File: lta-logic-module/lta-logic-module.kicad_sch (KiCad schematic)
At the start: 9 parts

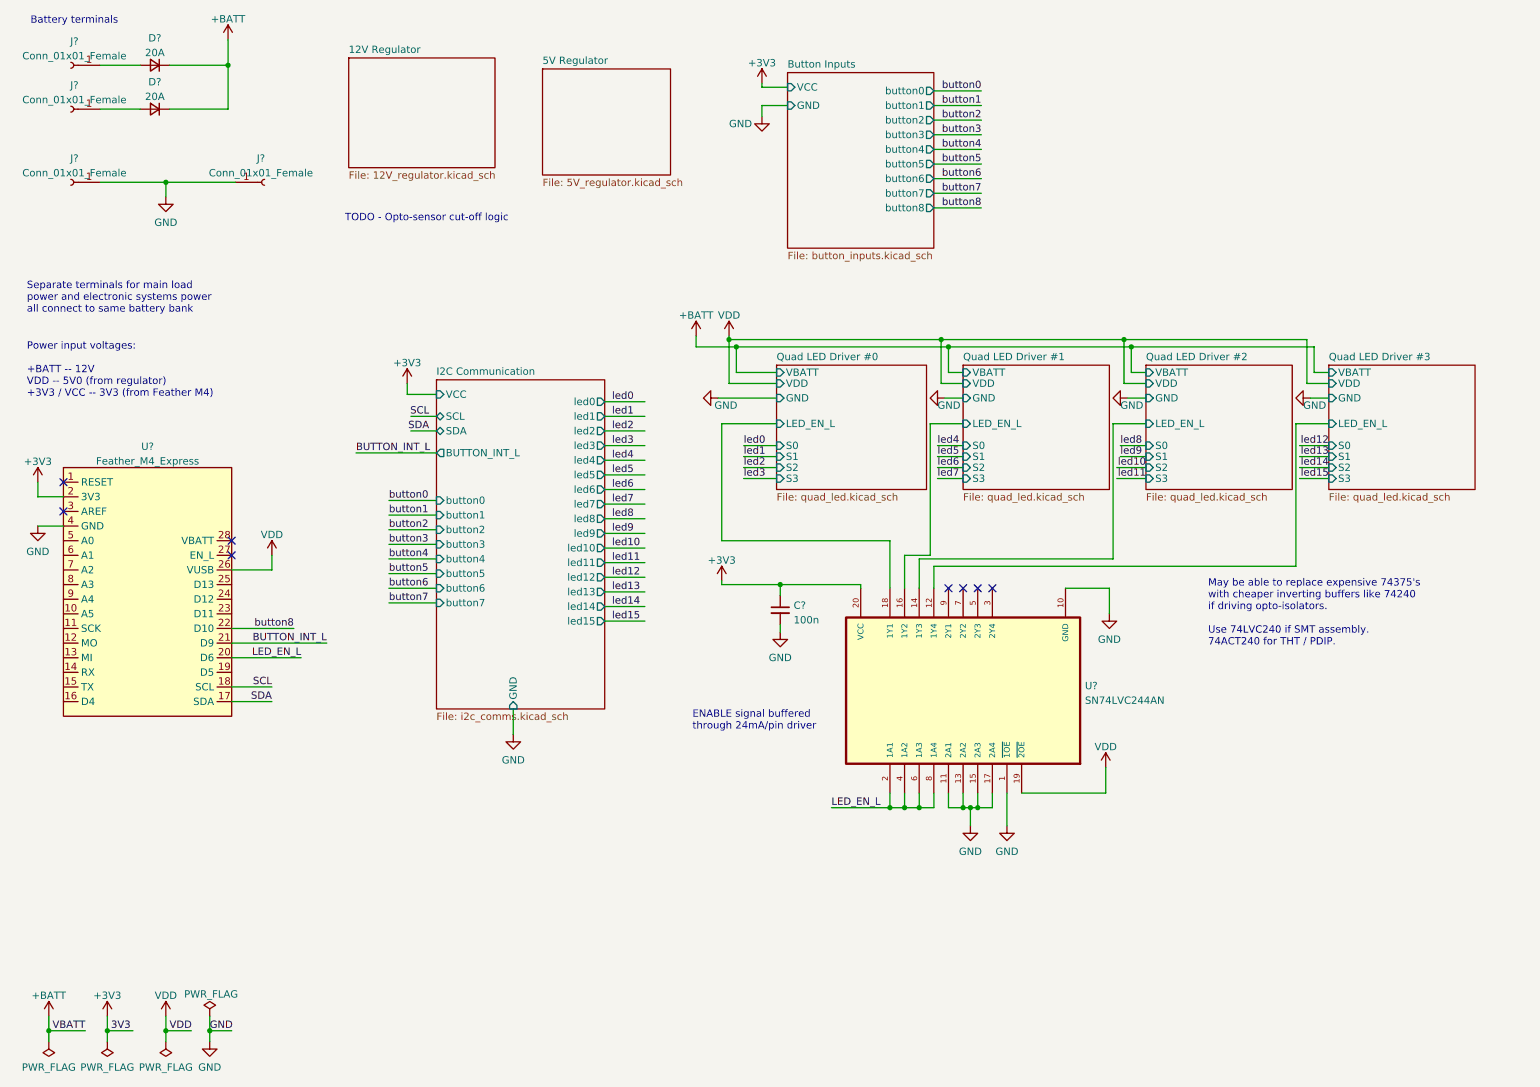
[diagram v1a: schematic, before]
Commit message: Full sketch of logic module schematic.
- Add button inputs
- Add LED signal driver / PWM combination
- Add 5V regulator based on LM2592
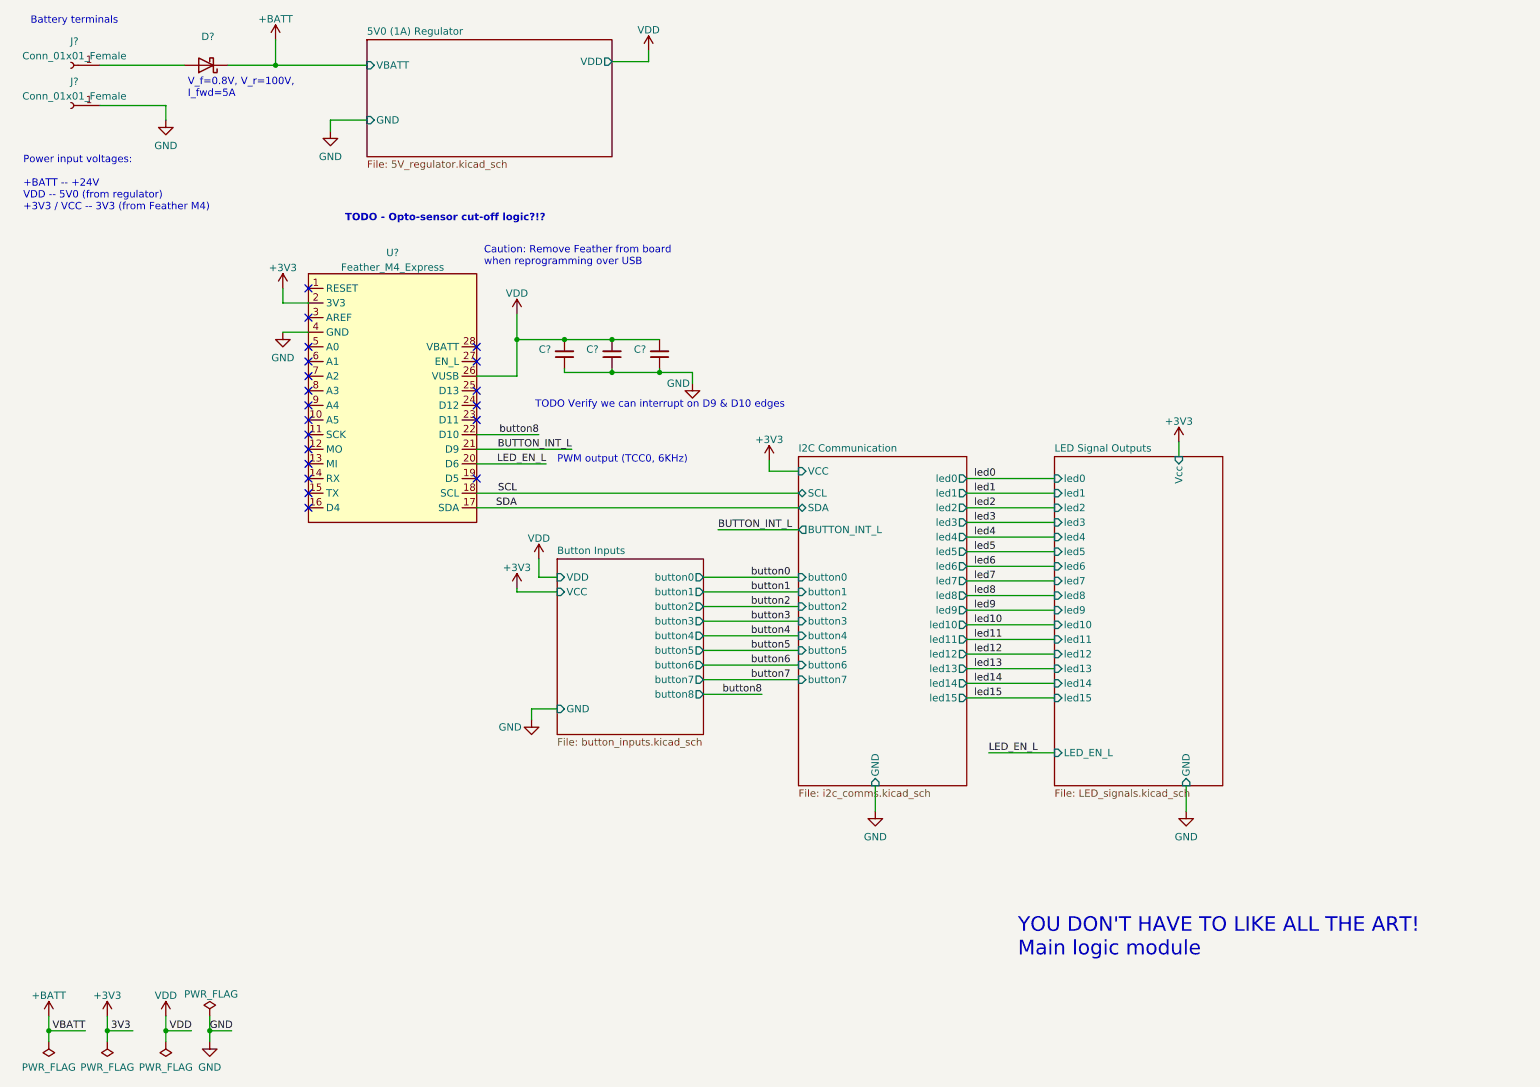
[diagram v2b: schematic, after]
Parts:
- removed C?: 100n, symbol Device:C_Small
- removed D? (x2): 20A, symbol Device:D_Small
- removed J? (x2): Conn_01x01_Female, symbol Connector:Conn_01x01_Female
- removed U?: SN74LVC244AN, Aaron_TI_Parts:TI_N_R-PDIP-T20, symbol Aaron-TI-Buffers:SN74LVC244AN
- added C? (x3): (no value), symbol Device:C_Small
- added D?: (no value), symbol Device:D_Schottky
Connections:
- net +BATT: now also D?.1 (K)
- net GND: now also C?.1, C?.1, C?.1
- net VDD: now also C?.2, C?.2, C?.2
- net at J?.1 (Pin_1): now also D?.2 (A)
- no-connect marks 8 -> 20
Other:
- sheet 5V Regulator renamed 5V0 (1A) Regulator
- removed sheet 12V Regulator
- removed sheet Quad LED Driver #0
- removed sheet Quad LED Driver #1
- removed sheet Quad LED Driver #2
- removed sheet Quad LED Driver #3
- added sheet LED Signal Outputs (LED_signals.kicad_sch)
- sheet 5V0 (1A) Regulator ports: added GND, VBATT, VDD; removed none
- sheet Button Inputs ports: added VDD; removed none
- note added: "Caution: Remove Feather from board when reprogramming over USB"
- note added: "PWM output (TCC0, 6KHz)"
- note added: "Power input voltages: +BATT -- +24V VDD -- 5V0 (from regulator) +3V3 / VCC -- 3V3 (from Feather M4)"
- note added: "TODO - Opto-sensor cut-off logic?!?"
- note added: "TODO Verify we can interrupt on D9 & D10 edges"
- note added: "V_f=0.8V, V_r=100V, I_fwd=5A"
- note added: "YOU DON'T HAVE TO LIKE ALL THE ART! Main logic module"
- note removed: "ENABLE signal buffered through 24mA/pin driver"
- note removed: "May be able to replace expensive 74375's with cheaper inverting buffers like 74240 if driving opto-isolators. Use 74LVC240 if SMT assembly. 74ACT240 for THT / PDIP."
- note removed: "Power input voltages: +BATT -- 12V VDD -- 5V0 (from regulator) +3V3 / VCC -- 3V3 (from Feather M4)"
- note removed: "Separate terminals for main load power and electronic systems power all connect to same battery bank"
- note removed: "TODO - Opto-sensor cut-off logic"
- moved on the sheet: J?, U?

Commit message: Fix ERC violations.
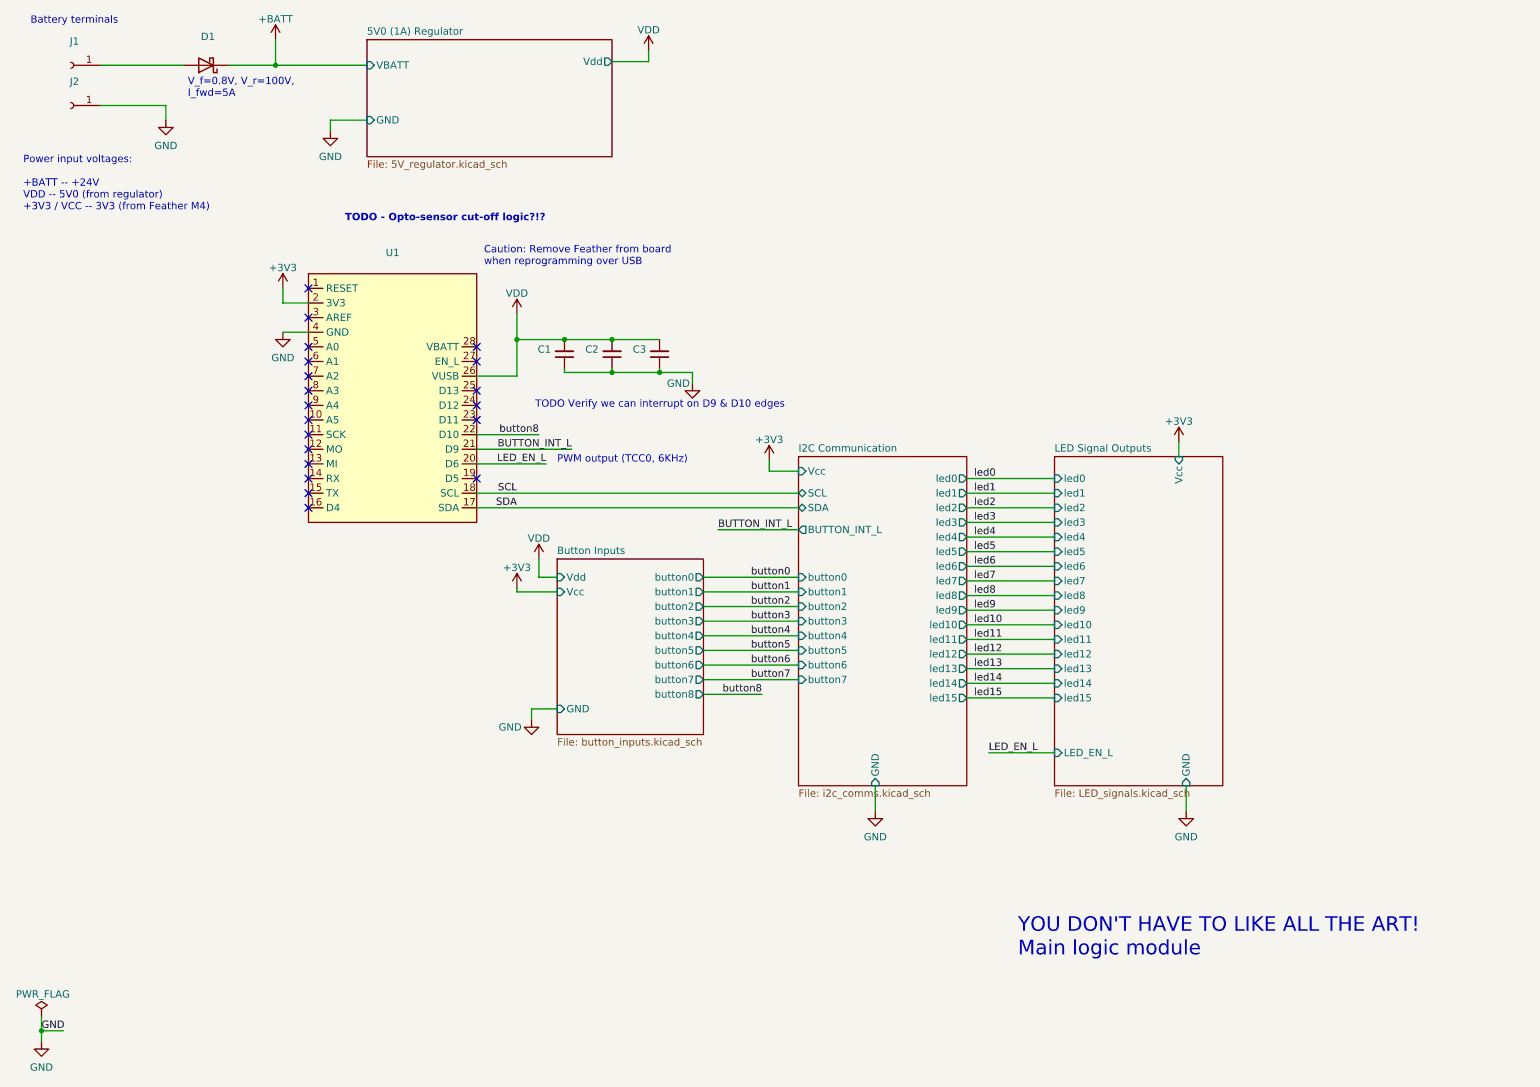
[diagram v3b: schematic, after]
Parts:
- J1, J2: renamed from J?; value Conn_01x01_Female -> (none)
- U1: renamed from U?; value Feather_M4_Express -> (none); footprint aaron-imported-parts:Arduino_Feather_M4_Express_PinHeaders -> (none)
- gave numbers to parts that had none: 4
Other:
- sheet 5V0 (1A) Regulator ports: added Vdd; removed VDD
- sheet Button Inputs ports: added Vcc, Vdd; removed VCC, VDD
- sheet I2C Communication ports: added Vcc; removed VCC

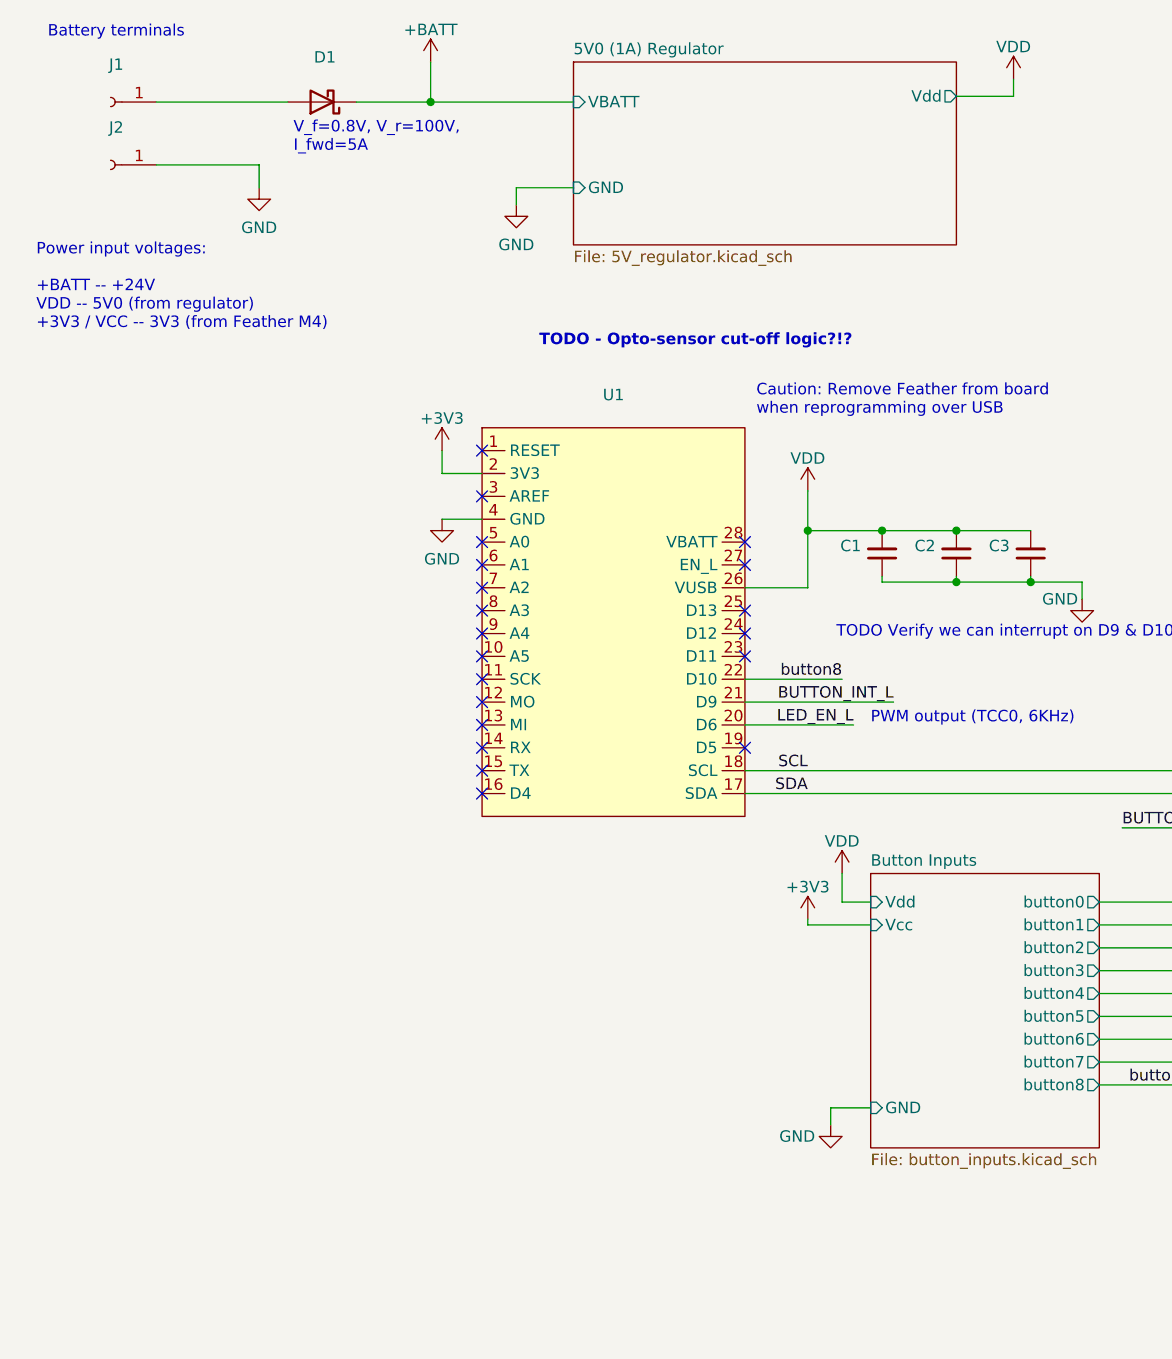
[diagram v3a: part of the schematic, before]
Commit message: Add TODOs, update some footprints.
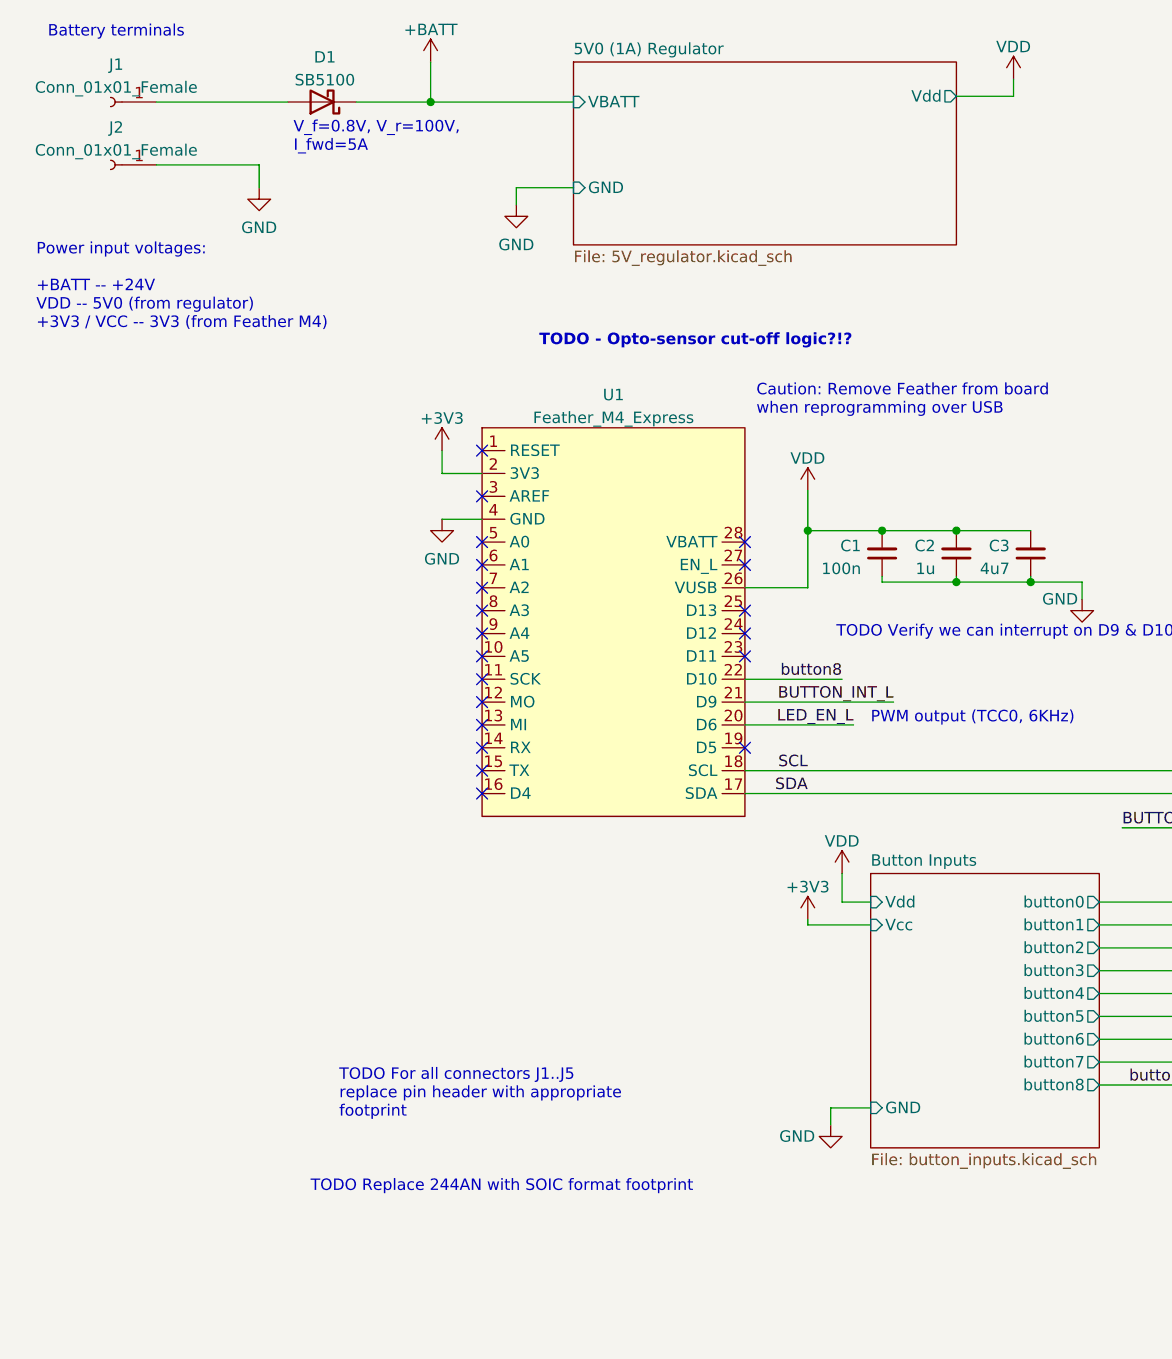
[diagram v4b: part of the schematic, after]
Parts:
- C1: value (none) -> 100n; footprint (none) -> Capacitor_SMD:C_0603_1608Metric; Comment (none) -> 100nF 5% 6.3V 0603 X7R ceramic; 20mOhm < ESR < 10 Ohm; MANUFACTURER (none) -> KYOCERA; MPN (none) -> 06036C104JAT2A
- C2: value (none) -> 1u; footprint (none) -> Capacitor_SMD:C_0603_1608Metric; Comment (none) -> 1u 5% 16V 0603 X7R ceramic; 20mOhm < ESR < 10 Ohm; MANUFACTURER (none) -> KYOCERA; MPN (none) -> 0603YC105JAT2A
- C3: value (none) -> 4u7; footprint (none) -> Capacitor_SMD:C_0805_2012Metric; Comment (none) -> 4u7 5% 16V 0805 X7R ceramic; 20mOhm < ESR < 10 Ohm; MANUFACTURER (none) -> KYOCERA; MPN (none) -> 0805YC475KAT2A
- D1: value (none) -> SB5100; footprint (none) -> Diode_THT:D_DO-201AD_P15.24mm_Horizontal
- J1, J2: value (none) -> Conn_01x01_Female; footprint (none) -> Connector_PinHeader_2.54mm:PinHeader_1x01_P2.54mm_Vertical; Comment (none) -> TODO REPLACE FOOTPRINT; MPN (none) -> XXX TODO FIND
- U1: value (none) -> Feather_M4_Express; footprint (none) -> aaron-imported-parts:Arduino_Feather_M4_Express_PinHeaders; Comment (none) -> Use 1x16 and 1x12 female THT headers 2.54mm pitch
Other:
- note added: "TODO For all connectors J1..J5 replace pin header with appropriate footprint"
- note added: "TODO Replace 244AN with SOIC format footprint"

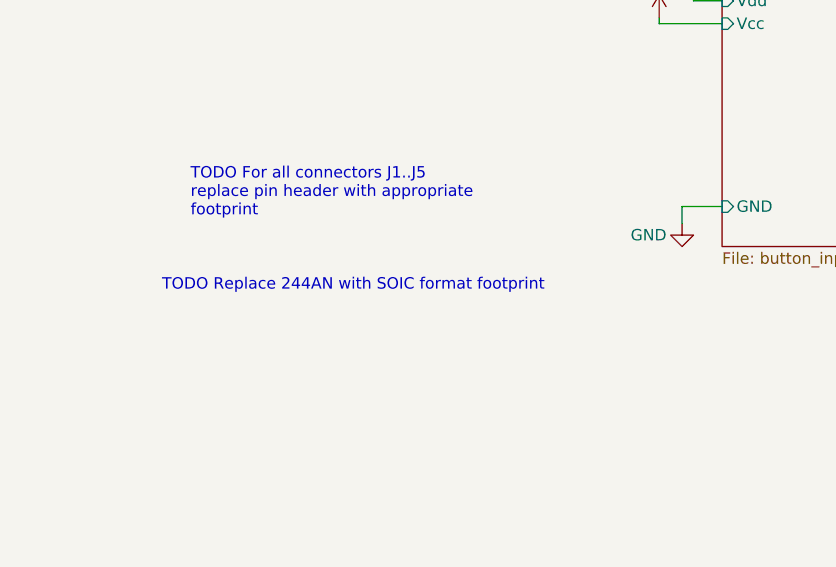
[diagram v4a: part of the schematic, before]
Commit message: Initial PCB setup
* Configure Elecrow DRC checks for lta-logic-module.
* Switch SN74LVC244A from 'N' PDIP to 'DWR' SOIC footprint.
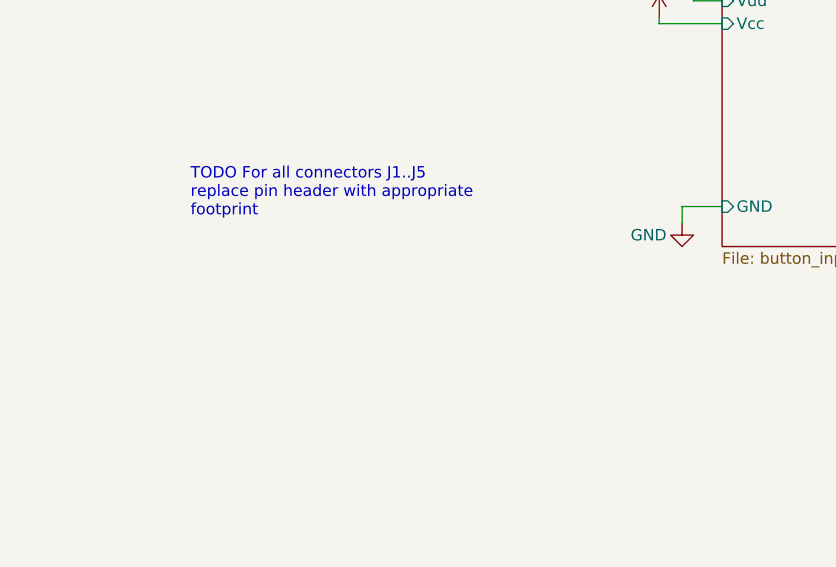
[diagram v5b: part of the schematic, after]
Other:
- note removed: "TODO Replace 244AN with SOIC format footprint"
